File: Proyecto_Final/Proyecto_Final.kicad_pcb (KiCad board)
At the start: 2 copper layers, 68.6 x 53.3 mm, 97 parts, among them J1 Conn_01x10, J10 Conn_01x02, J2 Conn_01x08, J3 USB_OTG, J4 Conn_01x08, J5 Conn_01x06, J6 Conn_01x02, J7 Conn_01x02, J8 Conn_02x03_Odd_Even, J9 Conn_02x03_Odd_Even, Q1 MMBT3904, Q2 MMBT3904, Q3 MMBT3904, Q4 MMBT3904, Q5 MMBT3904, Q6 MMBT3904, SW1 SW_Push, SW2 SW_Push, SW3 SW_Push, SW4 SW_Push, SW5 SW_Push, SW6 SW_Push, U1 TPS61087DSCR, U2 LM1117-3.3, U3 L293D, U4 FT232RL, U5 ATXMEGA32A4U-AU, U6 HC-05

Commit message: inicio del diseño PCB
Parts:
- C1, C12, C13, C14, C15, C16, C17, C2, C5, C6, C8, C9: footprint Capacitors_SMD:C_0805_HandSoldering -> Capacitor_SMD:C_0805_2012Metric; moved to F.Cu
- C10, C3: footprint Capacitors_SMD:CP_Elec_4x4.5 -> Capacitor_SMD:CP_Elec_4x4.5
- C11, C18, C4: footprint Capacitors_SMD:C_0805_HandSoldering -> Capacitor_SMD:C_0805_2012Metric
- C7: footprint Capacitors_SMD:CP_Elec_4x5.3 -> Capacitor_SMD:CP_Elec_4x5.3
- D1, D2, D8: footprint Diodes_SMD:D_SMA -> Diode_SMD:D_SMA; moved to F.Cu
- D10, D11, D12, D13, D3, D4, D5, D6, D9: footprint LEDs:LED_0805_HandSoldering -> LED_SMD:LED_0805_2012Metric
- D7: footprint LEDs:LED_D5.0mm-4 -> LED_SMD:LED_RGB_Cree-PLCC-6_6x5mm_P2.1mm
- J1: footprint Pin_Headers:Pin_Header_Straight_1x10_Pitch2.54mm -> Connector_PinSocket_2.54mm:PinSocket_1x10_P2.54mm_Vertical
- J10: footprint Pin_Headers:Pin_Header_Straight_1x02_Pitch2.54mm -> Connector_PinHeader_2.54mm:PinHeader_1x02_P2.54mm_Vertical
- J2, J4: footprint Pin_Headers:Pin_Header_Straight_1x08_Pitch2.54mm -> Connector_PinSocket_2.54mm:PinSocket_1x08_P2.54mm_Vertical
- J3: footprint Connectors:USB_Mini-B -> Connector_USB:USB_Micro-B_Molex_47346-0001
- J5: footprint Pin_Headers:Pin_Header_Straight_1x06_Pitch2.54mm -> Connector_PinSocket_2.54mm:PinSocket_1x06_P2.54mm_Vertical
- J6, J7: footprint TerminalBlocks_Phoenix:TerminalBlock_Phoenix_MPT-2.54mm_2pol -> TerminalBlock_Phoenix:TerminalBlock_Phoenix_MPT-0,5-2-2.54_1x02_P2.54mm_Horizontal
- J8, J9: footprint Pin_Headers:Pin_Header_Straight_2x03_Pitch2.54mm -> Connector_PinSocket_2.54mm:PinSocket_2x03_P2.54mm_Vertical
- Q1, Q2, Q3, Q4, Q5, Q6: footprint TO_SOT_Packages_SMD:SOT-23_Handsoldering -> Package_TO_SOT_SMD:SOT-23; moved to F.Cu
- R1, R10, R11, R12, R13, R14, R15, R16, R17, R18, R19, R2, R20, R21, R22, R23, R24, R25, R26, R27, R28, R29, R30, R32, R33, R34, R36, R6, R7, R8, R9: footprint Resistors_SMD:R_1206_HandSoldering -> Resistor_SMD:R_1206_3216Metric; moved to F.Cu
- R3, R31, R35, R4, R5: footprint Resistors_SMD:R_1206_HandSoldering -> Resistor_SMD:R_1206_3216Metric
- RV1: footprint Potentiometers:Potentiometer_Trimmer_Bourns_PV36W -> Potentiometer_THT:Potentiometer_Bourns_3339P_Vertical
- SW1, SW2, SW3, SW4, SW5, SW6: footprint Buttons_Switches_SMD:SW_SPST_FSMSM -> Button_Switch_SMD:SW_SPST_FSMSM
- U1, U4: moved to F.Cu
- U2: footprint TO_SOT_Packages_SMD:TO-252-2 -> Package_TO_SOT_SMD:TO-252-2; moved to F.Cu
- U5: footprint Housings_QFP:TQFP-44_10x10mm_Pitch0.8mm -> Package_QFP:TQFP-44_10x10mm_P0.8mm
- U6: value HC-05 -> MODULE-BLUETOOTH-HC-05(34P-27X13MM); footprint Platzi:HC-05 -> HC-05:BLUETOOTH-HC-05
- moved D3 211.1 mm to (48.3, 122.9)
- moved U2 197.8 mm to (58.5, 112.2), turned to 0 degrees
- moved C7 189.5 mm to (69.1, 117.9)
- moved SW4 181.8 mm to (76.0, 89.3), turned to 0 degrees
- moved SW6 179.3 mm to (70.9, 102.1), turned to 0 degrees
- moved R16 179.3 mm to (72.6, 121.5), turned to 0 degrees
- moved D9 178.7 mm to (76.7, 123.4), turned to 0 degrees
- moved C3 175.6 mm to (88.4, 99.9), turned to 0 degrees
- moved D8 175.3 mm to (79.8, 107.8)
- moved R9 175.1 mm to (84.0, 115.3), turned to 0 degrees
- moved SW3 174.4 mm to (58.9, 102.6), turned to 0 degrees
- moved SW2 171.9 mm to (76.0, 85.2), turned to 0 degrees
- moved D6 171.7 mm to (88.0, 116.0)
- moved C9 169.2 mm to (86.8, 118.0), turned to 0 degrees
- moved D4 169.1 mm to (91.5, 113.7)
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
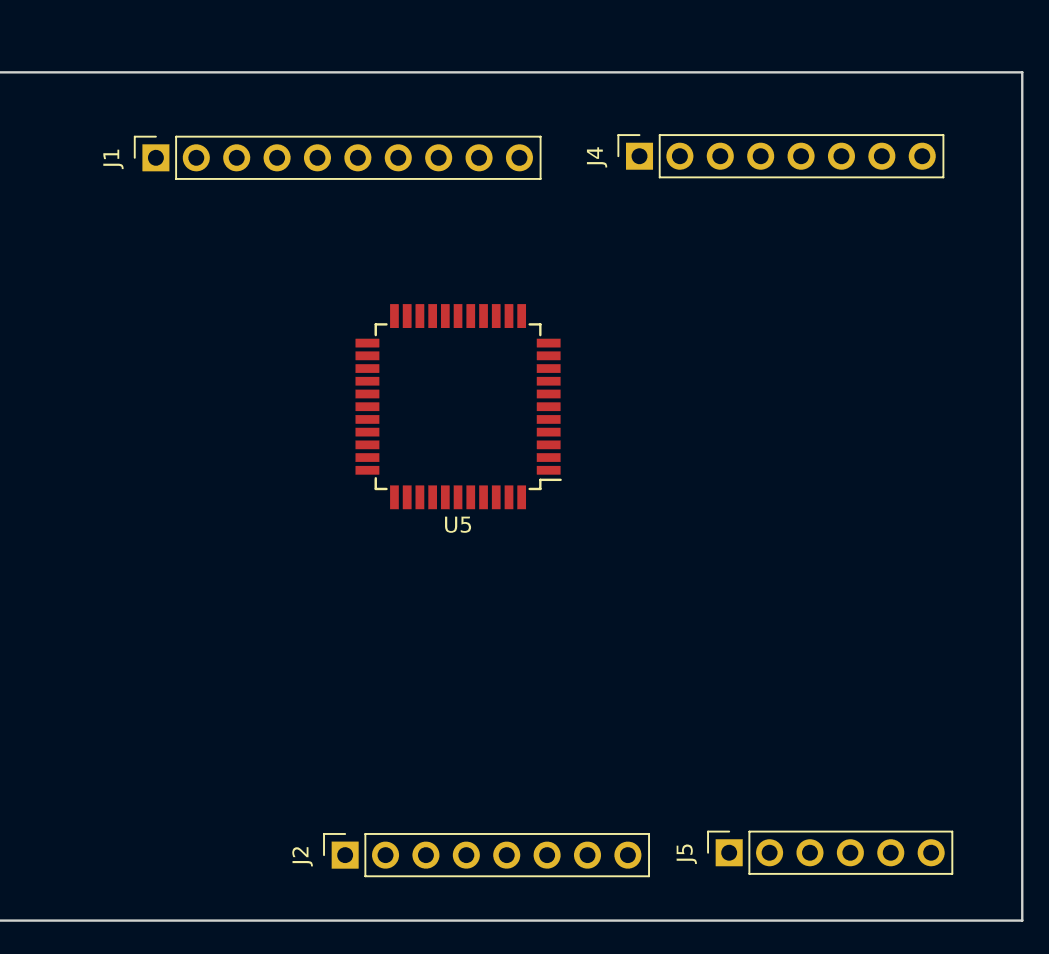
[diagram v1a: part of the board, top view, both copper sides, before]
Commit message: ubicacion perfecta de regletas shield arduino
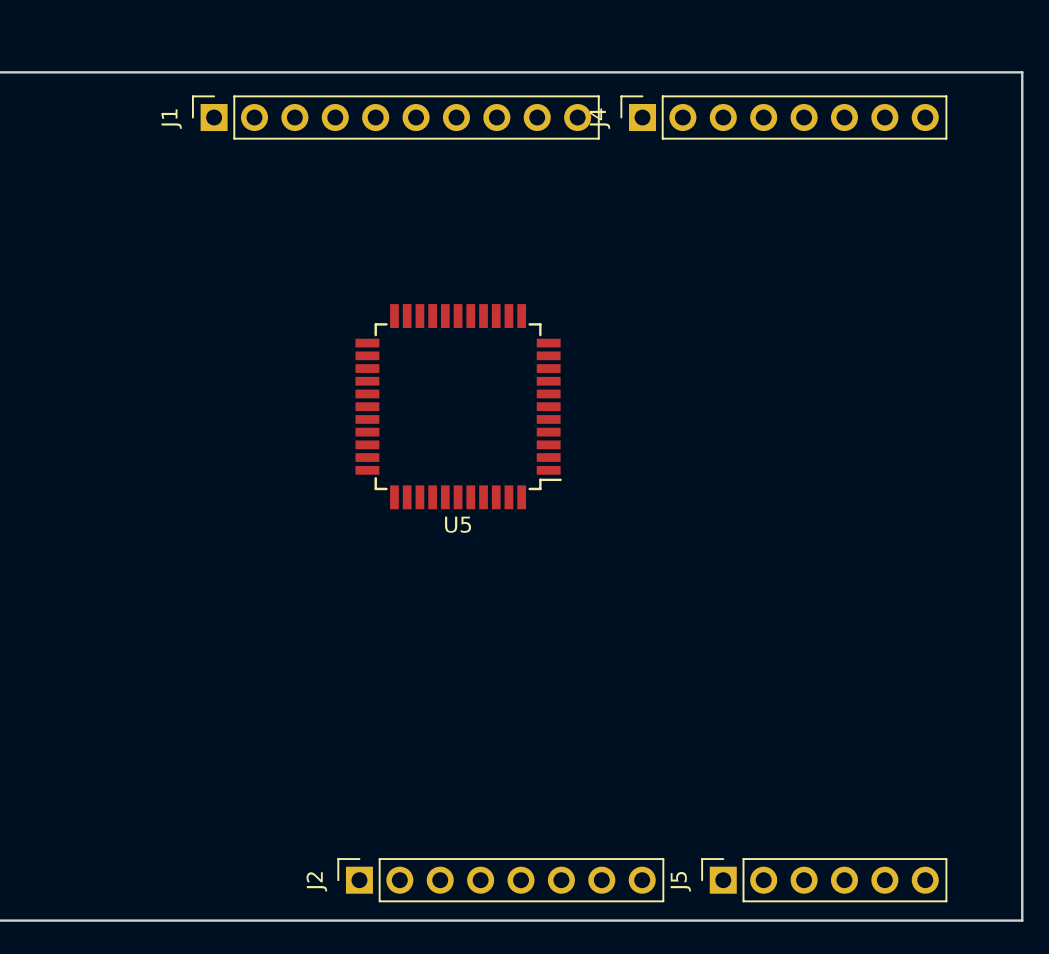
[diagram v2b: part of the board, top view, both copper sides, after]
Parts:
- moved J1 4.45 mm to (140.0, 80.5)
- moved J4 2.44 mm to (166.9, 80.5)
- moved J2 1.81 mm to (149.1, 128.4)
- moved J5 1.77 mm to (172.0, 128.4)
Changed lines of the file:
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@@
   (general
     (thickness 1.6)
-    (drawings 6)
+    (drawings 12)
     (tracks 0)
     (zones 0)
@@
   )
   (module Connector_PinSocket_2.54mm:PinSocket_1x10_P2.54mm_Vertical (layer F.Cu)
-    (at 136.3 83 90)
+    (at 139.959 80.466 90)
     (descr "Through hole straight socket strip, 1x10, 2.54mm pitch, single row (from Kicad 4.0.7), script generated")
     (tags "Through hole socket strip THT 1x10 2.54mm single row")
@@
   )
   (module Connector_PinSocket_2.54mm:PinSocket_1x08_P2.54mm_Vertical (layer F.Cu)
-    (at 148.2 126.85 90)
+    (at 149.099 128.426 90)
     (descr "Through hole straight socket strip, 1x08, 2.54mm pitch, single row (from Kicad 4.0.7), script generated")
     (tags "Through hole socket strip THT 1x08 2.54mm single row")
@@
   )
   (module Connector_PinSocket_2.54mm:PinSocket_1x08_P2.54mm_Vertical (layer F.Cu)
-    (at 166.71 82.9 90)
+    (at 166.899 80.466 90)
     (descr "Through hole straight socket strip, 1x08, 2.54mm pitch, single row (from Kicad 4.0.7), script generated")
     (tags "Through hole socket strip THT 1x08 2.54mm single row")
@@
   )
   (module Connector_PinSocket_2.54mm:PinSocket_1x06_P2.54mm_Vertical (layer F.Cu)
-    (at 172.35 126.7 90)
+    (at 171.979 128.426 90)
     (descr "Through hole straight socket strip, 1x06, 2.54mm pitch, single row (from Kicad 4.0.7), script generated")
     (tags "Through hole socket strip THT 1x06 2.54mm single row")
@@
       (net 77 "Net-(R35-Pad1)"))
   )
+  (dimension 4.080196 (width 0.3) (layer Dwgs.User)
+    (gr_text "4,080 mm" (at 164.860098 69.45) (layer Dwgs.User)
+      (effects (font (size 1.5 1.5) (thickness 0.3)))
+    )
+    (feature1 (pts (xy 166.900196 80.47) (xy 166.900196 70.963579)))
+    (feature2 (pts (xy 162.82 80.47) (xy 162.82 70.963579)))
+    (crossbar (pts (xy 162.82 71.55) (xy 166.900196 71.55)))
+    (arrow1a (pts (xy 166.900196 71.55) (xy 165.773692 72.136421)))
+    (arrow1b (pts (xy 166.900196 71.55) (xy 165.773692 70.963579)))
+    (arrow2a (pts (xy 162.82 71.55) (xy 163.946504 72.136421)))
+    (arrow2b (pts (xy 162.82 71.55) (xy 163.946504 70.963579)))
+  )
+  (dimension 44.720219 (width 0.3) (layer Dwgs.User)
+    (gr_text "44,720 mm" (at 144.53989 72.65) (layer Dwgs.User)
+      (effects (font (size 1.5 1.5) (thickness 0.3)))
+    )
+    (feature1 (pts (xy 122.179781 80.46) (xy 122.179781 74.163579)))
+    (feature2 (pts (xy 166.9 80.46) (xy 166.9 74.163579)))
+    (crossbar (pts (xy 166.9 74.75) (xy 122.179781 74.75)))
+    (arrow1a (pts (xy 122.179781 74.75) (xy 123.306285 74.163579)))
+    (arrow1b (pts (xy 122.179781 74.75) (xy 123.306285 75.336421)))
+    (arrow2a (pts (xy 166.9 74.75) (xy 165.773496 74.163579)))
+    (arrow2b (pts (xy 166.9 74.75) (xy 165.773496 75.336421)))
+  )
+  (dimension 50.496987 (width 0.3) (layer Dwgs.User)
+    (gr_text "50,500 mm" (at 199.44 105.718493 270) (layer Dwgs.User)
+      (effects (font (size 1.5 1.5) (thickness 0.3)))
+    )
+    (feature1 (pts (xy 184.68 130.966987) (xy 197.926421 130.966987)))
+    (feature2 (pts (xy 184.68 80.47) (xy 197.926421 80.47)))
+    (crossbar (pts (xy 197.34 80.47) (xy 197.34 130.966987)))
+    (arrow1a (pts (xy 197.34 130.966987) (xy 196.753579 129.840483)))
+    (arrow1b (pts (xy 197.34 130.966987) (xy 197.926421 129.840483)))
+    (arrow2a (pts (xy 197.34 80.47) (xy 196.753579 81.596504)))
+    (arrow2b (pts (xy 197.34 80.47) (xy 197.926421 81.596504)))
+  )
+  (dimension 2.54238 (width 0.3) (layer Dwgs.User)
+    (gr_text "2,540 mm" (at 194.99 129.70119 270) (layer Dwgs.User)
+      (effects (font (size 1.5 1.5) (thickness 0.3)))
+    )
+    (feature1 (pts (xy 184.68 130.97238) (xy 193.476421 130.97238)))
+    (feature2 (pts (xy 184.68 128.43) (xy 193.476421 128.43)))
+    (crossbar (pts (xy 192.89 128.43) (xy 192.89 130.97238)))
+    (arrow1a (pts (xy 192.89 130.97238) (xy 192.303579 129.845876)))
+    (arrow1b (pts (xy 192.89 130.97238) (xy 193.476421 129.845876)))
+    (arrow2a (pts (xy 192.89 128.43) (xy 192.303579 129.556504)))
+    (arrow2b (pts (xy 192.89 128.43) (xy 193.476421 129.556504)))
+  )
+  (dimension 49.807083 (width 0.3) (layer Dwgs.User)
+    (gr_text "49,800 mm" (at 147.076458 145.8) (layer Dwgs.User)
+      (effects (font (size 1.5 1.5) (thickness 0.3)))
+    )
+    (feature1 (pts (xy 122.172917 128.43) (xy 122.172917 144.286421)))
+    (feature2 (pts (xy 171.98 128.43) (xy 171.98 144.286421)))
+    (crossbar (pts (xy 171.98 143.7) (xy 122.172917 143.7)))
+    (arrow1a (pts (xy 122.172917 143.7) (xy 123.299421 143.113579)))
+    (arrow1b (pts (xy 122.172917 143.7) (xy 123.299421 144.286421)))
+    (arrow2a (pts (xy 171.98 143.7) (xy 170.853496 143.113579)))
+    (arrow2b (pts (xy 171.98 143.7) (xy 170.853496 144.286421)))
+  )
+  (dimension 26.920224 (width 0.3) (layer Dwgs.User)
+    (gr_text "26,920 mm" (at 135.639888 141.7) (layer Dwgs.User)
+      (effects (font (size 1.5 1.5) (thickness 0.3)))
+    )
+    (feature1 (pts (xy 122.179776 128.43) (xy 122.179776 140.186421)))
+    (feature2 (pts (xy 149.1 128.43) (xy 149.1 140.186421)))
+    (crossbar (pts (xy 149.1 139.6) (xy 122.179776 139.6)))
+    (arrow1a (pts (xy 122.179776 139.6) (xy 123.30628 139.013579)))
+    (arrow1b (pts (xy 122.179776 139.6) (xy 123.30628 140.186421)))
+    (arrow2a (pts (xy 149.1 139.6) (xy 147.973496 139.013579)))
+    (arrow2b (pts (xy 149.1 139.6) (xy 147.973496 140.186421)))
+  )
   (dimension 53.4 (width 0.3) (layer Dwgs.User)

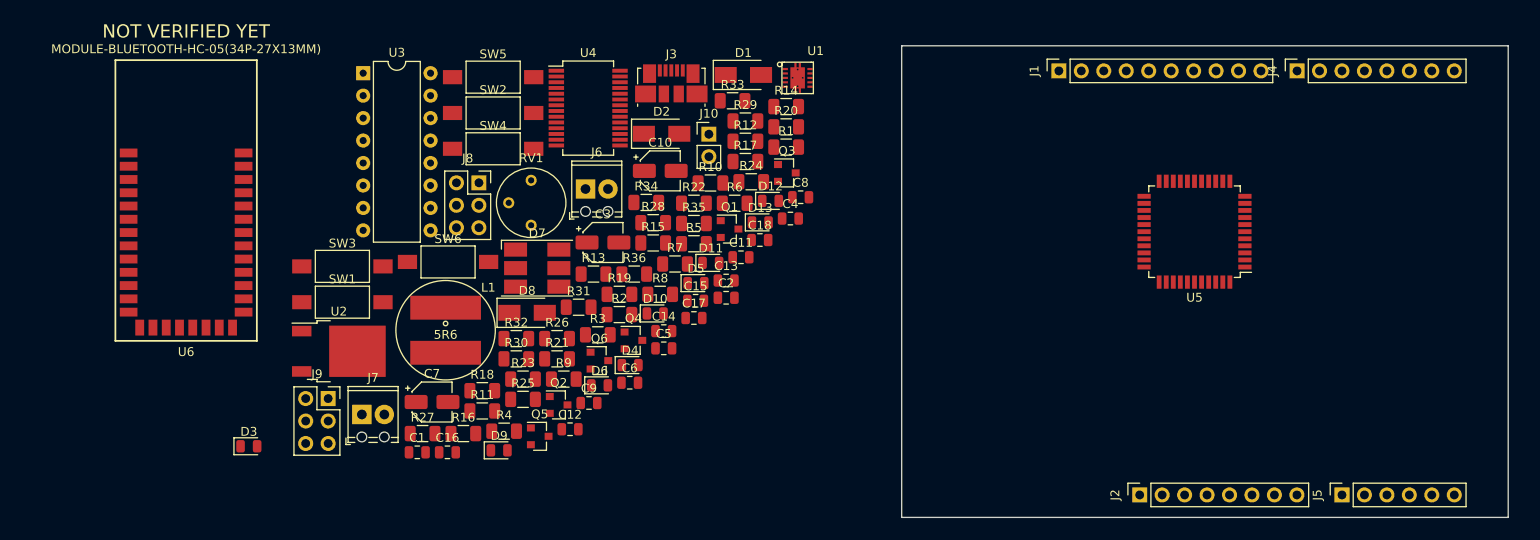
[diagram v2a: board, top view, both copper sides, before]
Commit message: posicion inicial de componentes
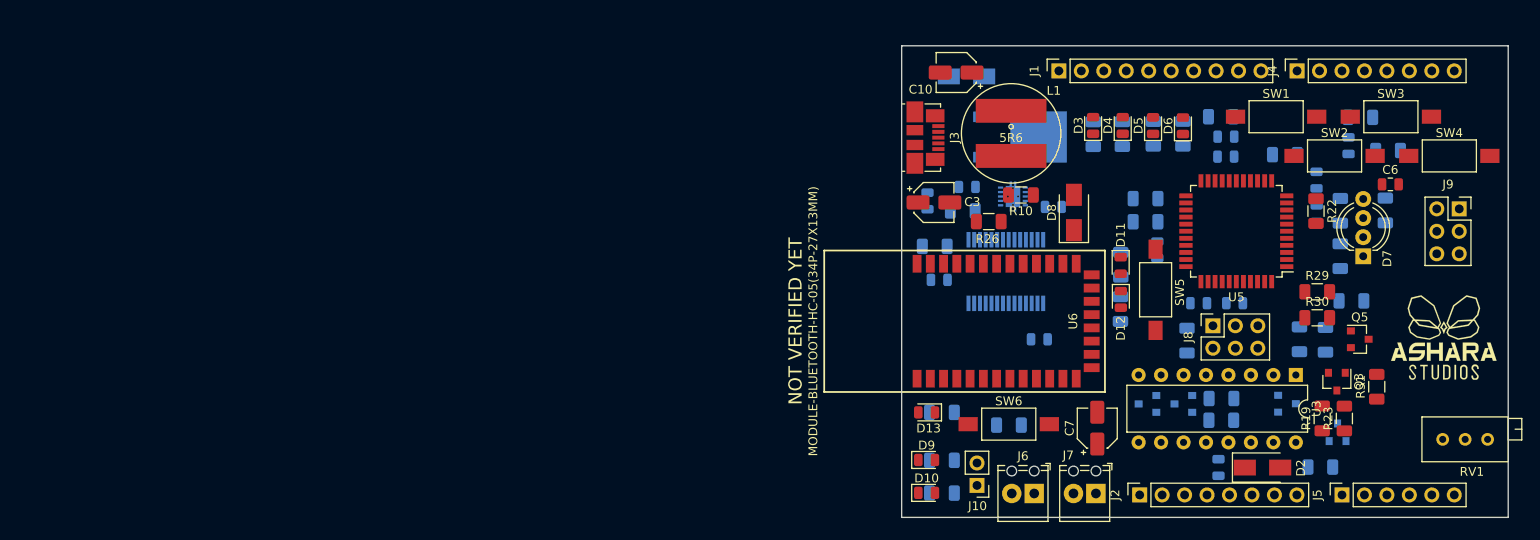
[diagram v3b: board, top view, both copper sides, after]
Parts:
- added G***: LOGO, LOGO, F.Cu at (183.5, 110.6)
- C1, C11, C12, C13, C14, C15, C16, C17, C18, C2, C4, C5, C8, C9, D1, Q1, Q2, Q4, Q6, R1, R11, R12, R13, R14, R15, R16, R17, R18, R2, R20, R21, R24, R25, R27, R28, R3, R32, R33, R34, R35, R36, R4, R5, R6, R7, R8, R9, U1, U2, U4: moved to B.Cu
- D7: footprint LED_SMD:LED_RGB_Cree-PLCC-6_6x5mm_P2.1mm -> LED_THT:LED_D5.0mm-4_RGB_Wide_Pins
- RV1: footprint Potentiometer_THT:Potentiometer_Bourns_3339P_Vertical -> Potentiometer_THT:Potentiometer_Bourns_3296X_Horizontal
- moved J9 129.7 mm to (185.2, 96.1)
- moved SW3 119.8 mm to (177.5, 85.7)
- moved U3 110.9 mm to (166.8, 114.9), turned to 270 degrees
- moved SW4 108.1 mm to (184.1, 90.1)
- moved SW1 107.7 mm to (164.5, 85.7)
- moved RV1 105.9 mm to (183.4, 122.1), turned to 180 degrees
- moved R11 104.7 mm to (174.1, 85.7), turned to 180 degrees
- moved D3 102.1 mm to (143.8, 86.6), turned to 90 degrees
- moved C1 98.2 mm to (158.9, 87.9)
- moved R4 97.8 mm to (171.8, 96.3), turned to 270 degrees
- moved R18 95.5 mm to (170.1, 110.9), turned to 270 degrees
- moved SW2 95.3 mm to (171.1, 90.1)
- moved D7 93.4 mm to (174.4, 101.4), turned to 90 degrees
- moved Q5 93.4 mm to (174.0, 110.8)
- moved R23 93.0 mm to (172.2, 119.8), turned to 90 degrees
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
